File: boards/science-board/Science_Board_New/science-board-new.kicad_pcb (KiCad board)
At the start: 4 copper layers, 70 x 70 mm, 14 parts, among them U1 Teensy4.1

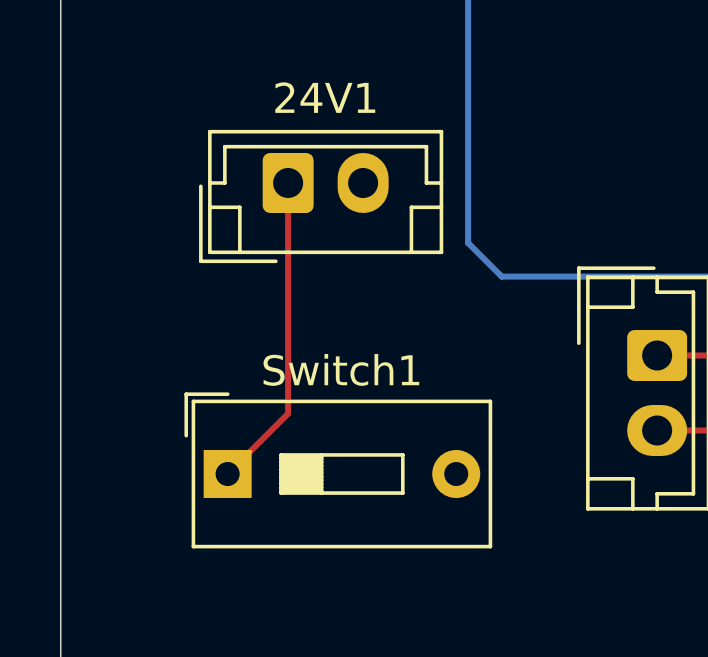
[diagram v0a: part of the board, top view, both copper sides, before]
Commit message: Added New Arm PCB
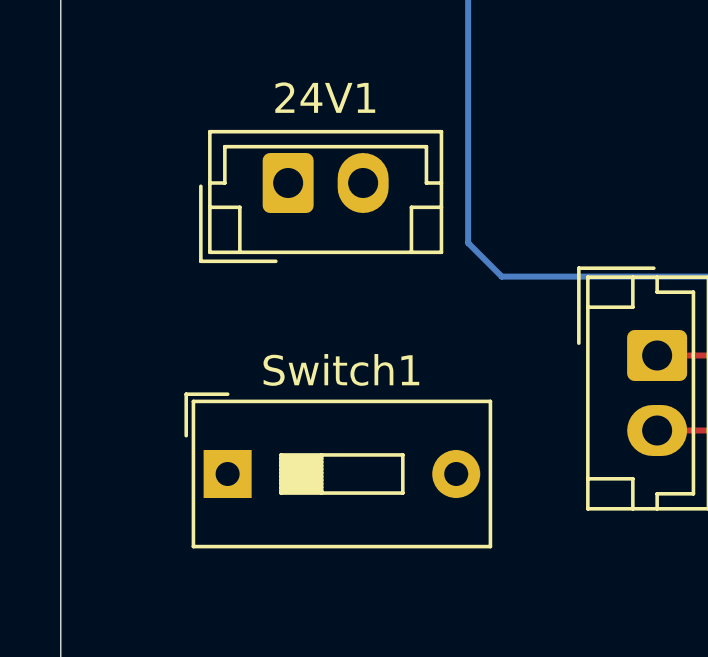
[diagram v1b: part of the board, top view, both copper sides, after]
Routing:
- net Net-(24V1-Pin_1): track 11.1 -> 0.57 mm
